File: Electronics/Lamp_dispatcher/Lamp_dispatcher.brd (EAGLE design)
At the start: 36.8 x 34.3 mm, 6 parts, among them X1 JST-XH-06-PIN-LONG-PAD, X2 JST-XH-02-PIN-LONG-PAD, X3 JST-XH-03-PIN-LONG-PAD, X4 JST-XH-03-PIN-LONG-PAD, X5 JST-XH-05-PIN-LONG-PAD, X6 JST-XH-05-PIN-LONG-PAD

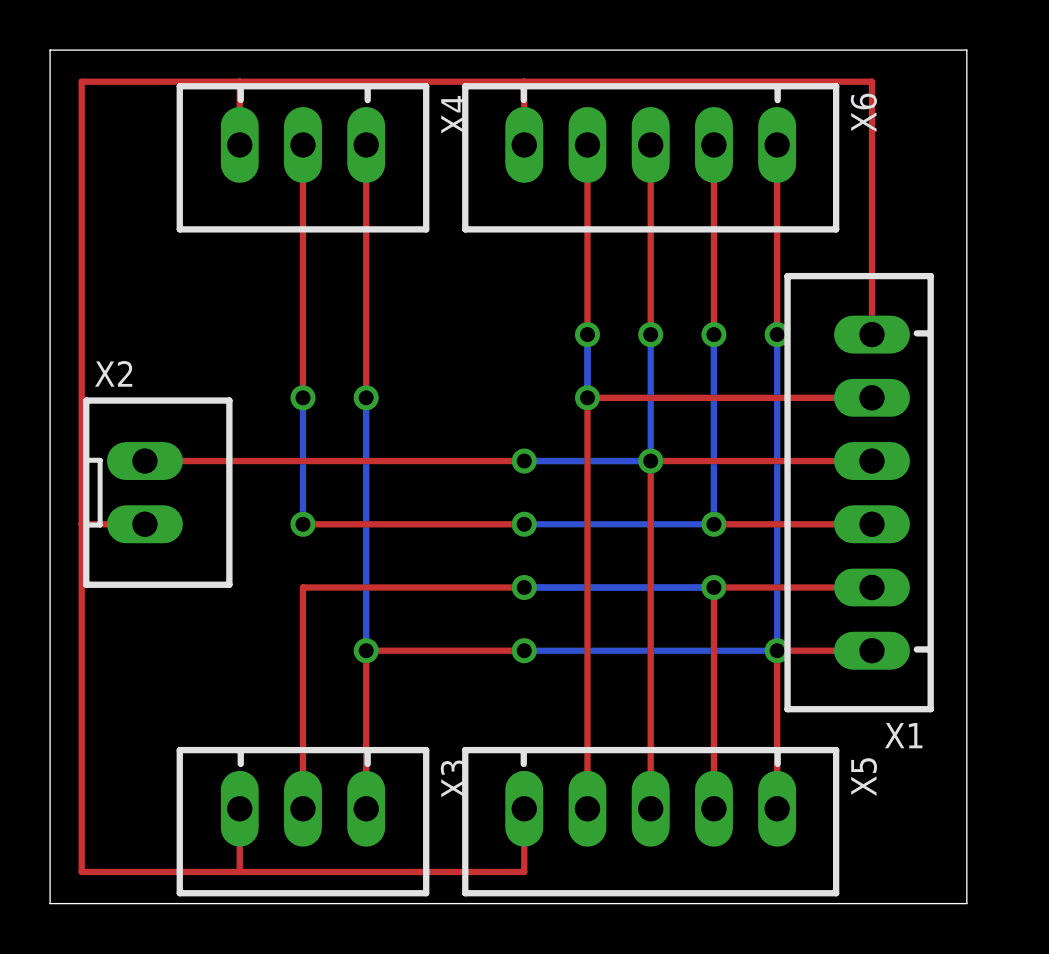
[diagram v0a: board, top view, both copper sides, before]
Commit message: Lamp dispatcher improved
What has been improved:
- rotated 2- and 6-pin JST connectors,
- corrected PCB dimensions,
- curved GND wire
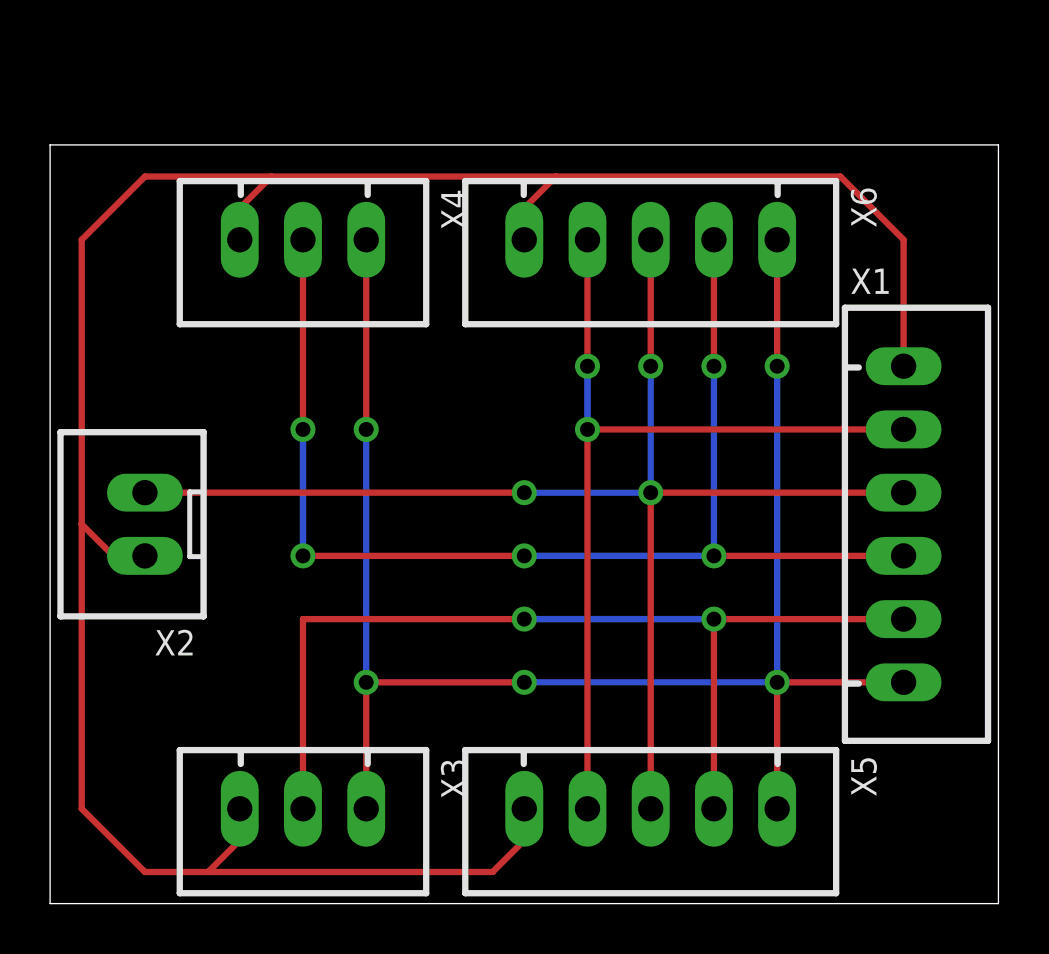
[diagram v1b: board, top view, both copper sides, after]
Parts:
- moved X4 3.81 mm to (10.2, 26.7)
- moved X6 3.81 mm to (24.1, 26.7)
- moved X1 1.80 mm to (34.3, 15.2), turned to 270 degrees
- moved X2 1.27 mm to (3.81, 15.2), turned to 90 degrees
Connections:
- net API_BRAKE: now also X1.3, X2.2; no longer X1.4, X2.1
- net API_START_ENGINE: now also X1.6; no longer X1.1
- net API_TURN_LEFT: now also X1.5; no longer X1.2
- net API_TURN_RIGHT: now also X1.4; no longer X1.3
- net API_WITHDRAW: now also X1.2; no longer X1.5
- net GND: now also X1.1, X2.1; no longer X1.6, X2.2
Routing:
- net GND: track 104.1 -> 96.0 mm
- net API_START_ENGINE: track 73.7 -> 67.3 mm
- net API_TURN_RIGHT: track 53.3 -> 49.5 mm
- net API_WITHDRAW: track 38.1 -> 35.6 mm
- net API_BRAKE: track 55.9 -> 53.3 mm
- net API_TURN_LEFT: track 40.6 -> 39.4 mm
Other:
- board size 36.8 x 34.3 mm -> 38.1 x 30.5 mm
